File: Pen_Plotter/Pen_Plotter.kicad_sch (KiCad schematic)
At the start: 37 parts, among them J1 USB_Type-C_Breakout, J2 PinHeader_01x05_P2.54mm_Verti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, J3 PinHeader_01x05_P2.54mm_Verti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, J4 Screw_Terminal_01x02_P3.5mm, J5 PinHeader_01x02_P2.54mm_Verti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, J6 PinHeader_01x02_P2.54mm_Verti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, J7 PinHeader_01x03_P2.54mm_Verti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, Q1 Transistor_MOSFET_NCh_SOT23, Q2 Transistor_MOSFET_NCh_SOT23, SW1 Switch_Tactile_Omron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

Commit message: Added some text
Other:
- note added: "ESP32 Wroom Module"
- note added: "Minimum Circuit"
- note added: "Motor 1"
- note added: "Motor 2"
- note added: "Voltage Regulator Circuit"
- moved on the sheet: C1, C2, C3, D1, R1, SW1, U1

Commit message: 6 January
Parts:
- J1: footprint ProshPlay:ProshPlay-Type-C-breakout-board -> Proshplay Type C:ProshPlay-Type-C-breakout-board
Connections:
- no-connect marks 7 -> 17
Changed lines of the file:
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@@
 	)
 	(junction
+		(at 328.93 125.73)
+		(diameter 0)
+		(color 0 0 0 0)
+	)
+	(junction
 		(at 256.54 111.76)
 		(diameter 0)
@@
 		(color 0 0 0 0)
 	)
+	(junction
+		(at 340.7823 109.855)
+		(diameter 0)
+		(color 0 0 0 0)
+	)
 	(no_connect
 		(at 341.63 45.72)
 	)
 	(no_connect
+		(at 195.58 90.17)
+	)
+	(no_connect
+		(at 165.1 82.55)
+	)
+	(no_connect
 		(at 372.11 43.18)
 	)
 	(no_connect
+		(at 195.58 92.71)
+	)
+	(no_connect
 		(at 341.63 66.04)
 	)
 	(no_connect
+		(at 195.58 95.25)
+	)
+	(no_connect
 		(at 341.63 58.42)
 	)
 	(no_connect
+		(at 195.58 97.79)
+	)
+	(no_connect
 		(at 341.63 63.5)
 	)
 	(no_connect
+		(at 195.58 125.73)
+	)
+	(no_connect
+		(at 195.58 130.81)
+	)
+	(no_connect
 		(at 372.11 63.5)
 	)
@@
 		(at 341.63 60.96)
 	)
+	(no_connect
+		(at 165.1 85.09)
+	)
+	(no_connect
+		(at 195.58 87.63)
+	)
+	(no_connect
+		(at 195.58 123.19)
+	)
 	(wire
 		(pts
@@
 	(wire
 		(pts
+			(xy 328.93 125.73) (xy 328.93 126.365)
+		)
+		(stroke
+			(width 0)
+			(type default)
+		)
+	)
+	(wire
+		(pts
 			(xy 260.35 153.67) (xy 264.16 153.67)
 		)
@@
 	(wire
 		(pts
+			(xy 332.74 125.73) (xy 328.93 125.73)
+		)
+		(stroke
+			(width 0)
+			(type default)
+		)
+	)
+	(wire
+		(pts
+			(xy 332.74 129.54) (xy 332.74 125.73)
+		)
+		(stroke
+			(width 0)
+			(type default)
+		)
+	)
+	(wire
+		(pts
 			(xy 337.82 50.8) (xy 341.63 50.8)
 		)
@@
 	(wire
 		(pts
-			(xy 328.93 125.095) (xy 328.93 126.365)
+			(xy 328.93 125.095) (xy 328.93 125.73)
 		)
 		(stroke
@@
 	(wire
 		(pts
+			(xy 340.7823 109.855) (xy 336.55 109.855)
+		)
+		(stroke
+			(width 0)
+			(type default)
+		)
+	)
+	(wire
+		(pts
 			(xy 326.39 125.095) (xy 328.93 125.095)
 		)
@@
 	(wire
 		(pts
-			(xy 344.17 109.855) (xy 336.55 109.855)
+			(xy 344.17 109.855) (xy 340.7823 109.855)
 		)
 		(stroke
@@
 		)
 	)
+	(wire
+		(pts
+			(xy 339.09 129.54) (xy 332.74 129.54)
+		)
+		(stroke
+			(width 0)
+			(type default)
+		)
+	)
 	(global_label "EN"
 		(shape input)
@@
 	(global_label "VDD"
 		(shape input)
-		(at 284.48 30.48 90)
+		(at 284.48 30.48 0)
 		(fields_autoplaced yes)
 		(effects
@@
 		)
 		(property "Intersheetrefs" "${INTERSHEET_REFS}"
-			(at 284.48 23.8662 90)
+			(at 291.0938 30.48 0)
 			(effects
 				(font
@@
 			)
 		)
-		(property "Footprint" "ProshPlay:ProshPlay-Type-C-breakout-board"
+		(property "Footprint" "Proshplay Type C:ProshPlay-Type-C-breakout-board"
 			(at 329.565 120.015 0)
 			(effects
@@
 	)
 	(symbol
+		(lib_id "fab:PWR_FLAG")
+		(at 340.7823 109.855 0)
+		(unit 1)
+		(exclude_from_sim no)
+		(in_bom yes)
+		(on_board yes)
+		(dnp no)
+		(fields_autoplaced yes)
+		(property "Reference" "#FLG01"
+			(at 340.7823 109.855 0)
+			(effects
+				(font
+					(size 1.27 1.27)
+				)
+				(hide yes)
+			)
+		)
+		(property "Value" "PWR_FLAG"
+			(at 340.7823 104.775 0)
+			(effects
+				(font
+					(size 1.27 1.27)
+				)
+			)
+		)
+		(property "Footprint" ""
+			(at 340.7823 109.855 0)
+			(effects
+				(font
+					(size 1.27 1.27)
+				)
+				(hide yes)
+			)
+		)
+		(property "Datasheet" "~"
+			(at 340.7823 109.855 0)
+			(effects
+				(font
+					(size 1.27 1.27)
+				)
+				(hide yes)
+			)
+		)
+		(property "Description" "Special symbol for telling ERC where power comes from"
+			(at 340.7823 109.855 0)
+			(effects
+				(font
+					(size 1.27 1.27)
+				)
+				(hide yes)
+			)
+		)
+		(pin "1"
+		)
+		(instances
+			(project ""
+				(path "/4e9b223a-cbc5-44ea-8094-5eb0dbc835d2"
+					(reference "#FLG01")
+					(unit 1)
+				)
+			)
+		)
+	)
+	(symbol
 		(lib_id "fab:Transistor_MOSFET_NCh_SOT23")
 		(at 378.46 101.6 0)
@@
 					(unit 1)
 				)
+			)
+		)
+	)
+	(symbol
+		(lib_id "fab:PWR_FLAG")
+		(at 339.09 129.54 0)
+		(unit 1)
+		(exclude_from_sim no)
+		(in_bom yes)
+		(on_board yes)
+		(dnp no)
+		(fields_autoplaced yes)
+		(property "Reference" "#FLG02"
+			(at 339.09 129.54 0)
+			(effects
+				(font
+					(size 1.27 1.27)
+				)
+				(hide yes)
+			)
+		)
+		(property "Value" "PWR_FLAG"
+			(at 339.09 124.46 0)
+			(effects
+				(font
+					(size 1.27 1.27)
+				)
+			)
+		)
+		(property "Footprint" ""
+			(at 339.09 129.54 0)
+			(effects
+				(font
+					(size 1.27 1.27)
+				)
+				(hide yes)
+			)
+		)
+		(property "Datasheet" "~"
+			(at 339.09 129.54 0)
+			(effects
+				(font
+					(size 1.27 1.27)
+				)
+				(hide yes)
+			)
+		)
+		(property "Description" "Special symbol for telling ERC where power comes from"
+			(at 339.09 129.54 0)
+			(effects
+				(font
+					(size 1.27 1.27)
+				)
+				(hide yes)
+			)
+		)
+		(pin "1"
+		)
+		(instances
+			(project "Pen_Plotter"
+				(path "/4e9b223a-cbc5-44ea-8094-5eb0dbc835d2"
+					(reference "#FLG02")
+					(unit 1)
+				)

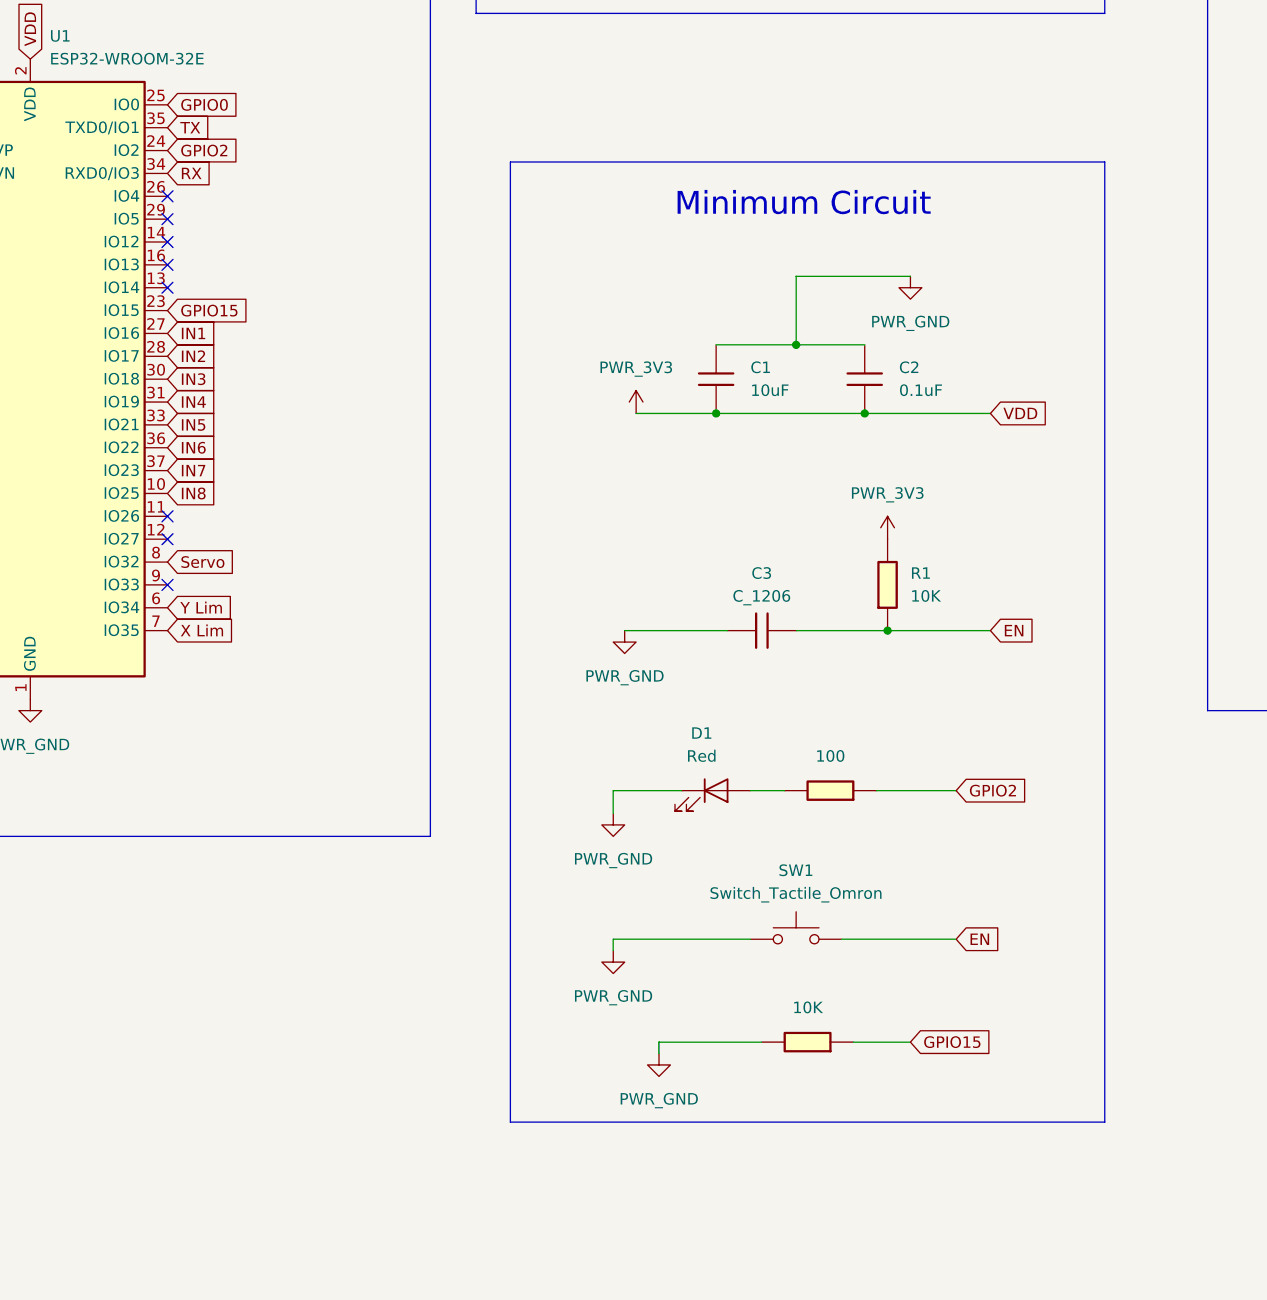
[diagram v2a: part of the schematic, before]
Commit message: Wired THT Components
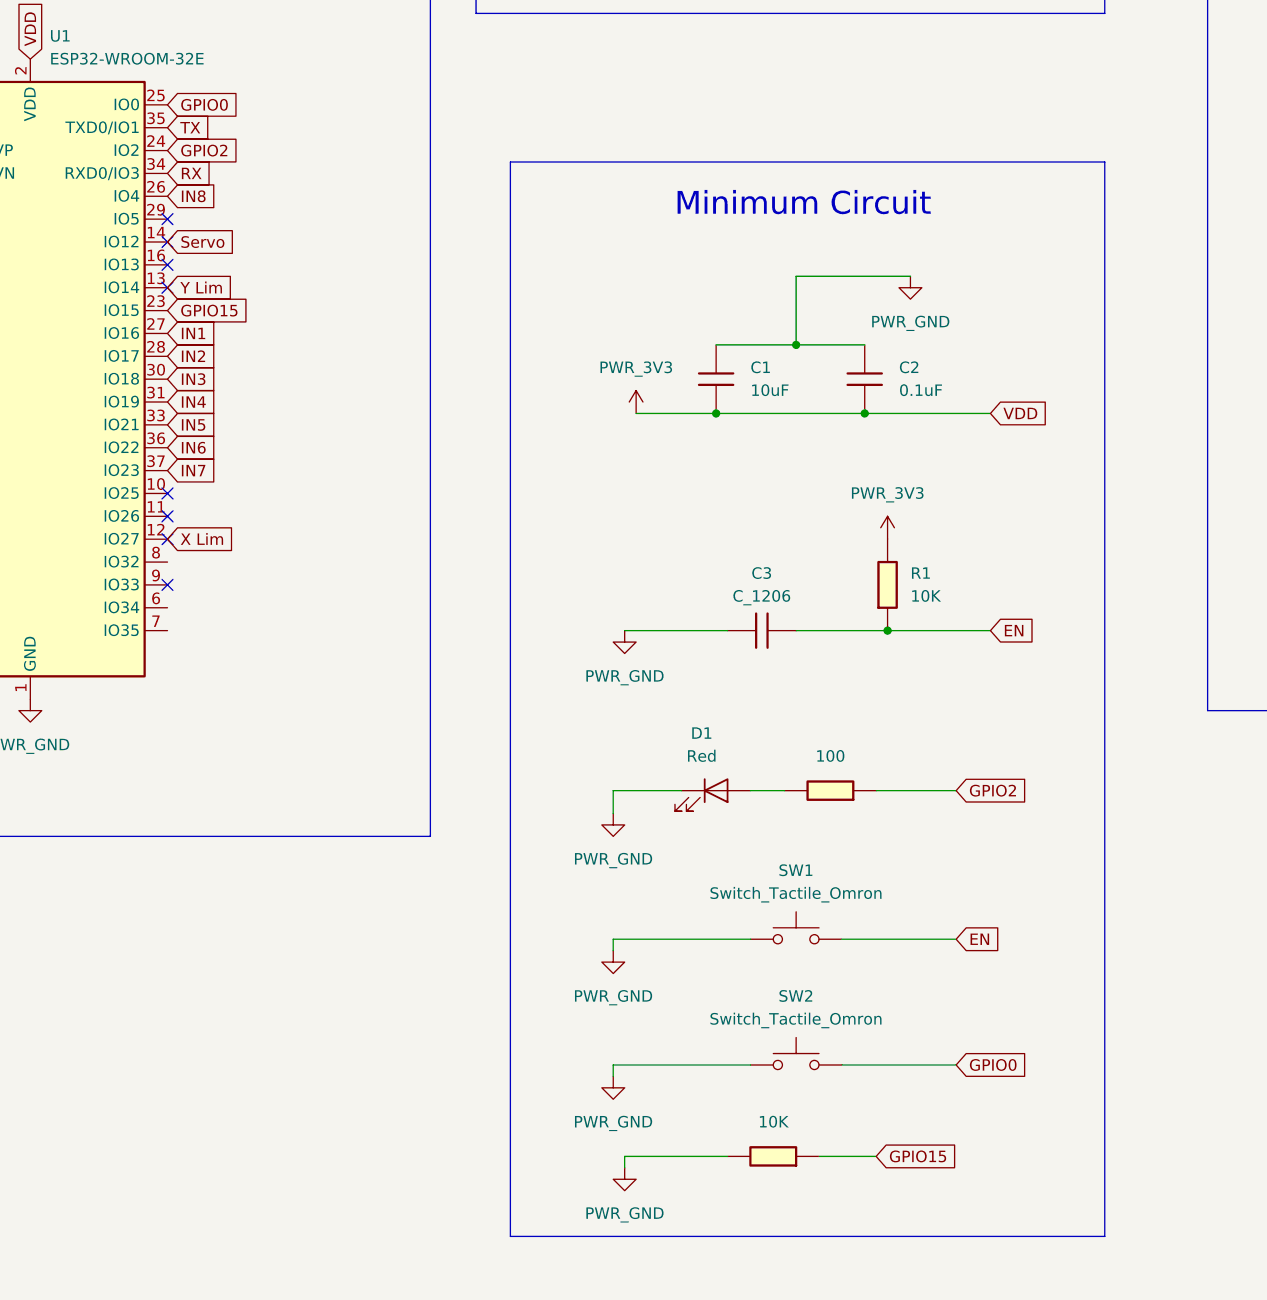
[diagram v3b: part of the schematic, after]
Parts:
- added SW2: Switch_Tactile_Omron, fab:Button_Omron_B3SN_6.0x6.0mm, symbol fab:Switch_Tactile_Omron
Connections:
- net GPIO0: now also SW2.2
- net IN8: now also U1.26 (IO4); no longer U1.10 (IO25)
- net PWR_GND: now also SW2.1
- net Servo: now also U1.14 (IO12); no longer U1.8 (IO32)
- net X Lim: now also U1.12 (IO27); no longer U1.7 (IO35)
- net Y Lim: now also U1.13 (IO14); no longer U1.6 (IO34)
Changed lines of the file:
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@@
 	(rectangle
 		(start 233.68 83.82)
-		(end 299.72 190.5)
+		(end 299.72 203.2)
 		(stroke
 			(width 0)
@@
 	)
 	(no_connect
+		(at 195.58 120.65)
+	)
+	(no_connect
 		(at 341.63 58.42)
 	)
 	(no_connect
+		(at 195.58 123.19)
+	)
+	(no_connect
 		(at 195.58 97.79)
 	)
@@
 		(at 165.1 85.09)
 	)
-	(no_connect
-		(at 195.58 87.63)
-	)
-	(no_connect
-		(at 195.58 123.19)
+	(wire
+		(pts
+			(xy 245.11 184.15) (xy 245.11 185.42)
+		)
+		(stroke
+			(width 0)
+			(type default)
+		)
 	)
 	(wire
@@
 	(wire
 		(pts
+			(xy 270.51 184.15) (xy 283.21 184.15)
+		)
+		(stroke
+			(width 0)
+			(type default)
+		)
+	)
+	(wire
+		(pts
 			(xy 254 35.56) (xy 254 41.91)
 		)
@@
 	(wire
 		(pts
-			(xy 250.19 181.61) (xy 261.62 181.61)
+			(xy 246.38 194.31) (xy 257.81 194.31)
 		)
 		(stroke
@@
 	(wire
 		(pts
-			(xy 250.19 182.88) (xy 250.19 181.61)
+			(xy 246.38 195.58) (xy 246.38 194.31)
 		)
 		(stroke
@@
 	(wire
 		(pts
+			(xy 260.35 184.15) (xy 245.11 184.15)
+		)
+		(stroke
+			(width 0)
+			(type default)
+		)
+	)
+	(wire
+		(pts
 			(xy 49.53 143.51) (xy 49.53 146.05)
 		)
@@
 	(wire
 		(pts
-			(xy 271.78 181.61) (xy 278.13 181.61)
+			(xy 267.97 194.31) (xy 274.32 194.31)
 		)
 		(stroke
@@
 	(global_label "Servo"
 		(shape input)
-		(at 195.58 128.27 0)
+		(at 195.58 92.71 0)
 		(fields_autoplaced yes)
 		(effects
@@
 		)
 		(property "Intersheetrefs" "${INTERSHEET_REFS}"
-			(at 203.7661 128.27 0)
+			(at 203.7661 92.71 0)
 			(effects
 				(font
@@
 		)
 	)
-	(global_label "IN8"
-		(shape input)
-		(at 195.58 120.65 0)
-		(fields_autoplaced yes)
-		(effects
-			(font
-				(size 1.27 1.27)
-			)
-			(justify left)
-		)
-		(property "Intersheetrefs" "${INTERSHEET_REFS}"
-			(at 201.71 120.65 0)
-			(effects
-				(font
-					(size 1.27 1.27)
-				)
-				(justify left)
-				(hide yes)
-			)
-		)
-	)
 	(global_label "OUT4"
 		(shape input)
@@
 		)
 	)
+	(global_label "IN8"
+		(shape input)
+		(at 195.58 87.63 0)
+		(fields_autoplaced yes)
+		(effects
+			(font
+				(size 1.27 1.27)
+			)
+			(justify left)
+		)
+		(property "Intersheetrefs" "${INTERSHEET_REFS}"
+			(at 201.71 87.63 0)
+			(effects
+				(font
+					(size 1.27 1.27)
+				)
+				(justify left)
+				(hide yes)
+			)
+		)
+	)
 	(global_label "IN4"
 		(shape input)
@@
 		)
 	)
+	(global_label "GPIO0"
+		(shape input)
+		(at 283.21 184.15 0)
+		(fields_autoplaced yes)
+		(effects
+			(font
+				(size 1.27 1.27)
+			)
+			(justify left)
+		)
+		(property "Intersheetrefs" "${INTERSHEET_REFS}"
+			(at 291.88 184.15 0)
+			(effects
+				(font
+					(size 1.27 1.27)
+				)
+				(justify left)
+				(hide yes)
+			)
+		)
+	)
 	(global_label "Y Lim"
 		(shape input)
-		(at 195.58 133.35 0)
+		(at 195.58 97.79 0)
 		(fields_autoplaced yes)
 		(effects
@@
 		)
 		(property "Intersheetrefs" "${INTERSHEET_REFS}"
-			(at 203.9476 133.35 0)
+			(at 203.9476 97.79 0)
 			(effects
 				(font
@@
 	(global_label "GPIO15"
 		(shape input)
-		(at 278.13 181.61 0)
+		(at 274.32 194.31 0)
 		(fields_autoplaced yes)
 		(effects
@@
 		)
 		(property "Intersheetrefs" "${INTERSHEET_REFS}"
-			(at 288.0095 181.61 0)
+			(at 284.1995 194.31 0)
 			(effects
 				(font
@@
 	(global_label "X Lim"
 		(shape input)
-		(at 195.58 135.89 0)
+		(at 195.58 125.73 0)
 		(fields_autoplaced yes)
 		(effects
@@
 		)
 		(property "Intersheetrefs" "${INTERSHEET_REFS}"
-			(at 204.0685 135.89 0)
+			(at 204.0685 125.73 0)
 			(effects
 				(font
@@
 	(symbol
 		(lib_id "fab:PWR_GND")
-		(at 250.19 182.88 0)
+		(at 246.38 195.58 0)
 		(unit 1)
 		(exclude_from_sim no)
@@
 		(fields_autoplaced yes)
 		(property "Reference" "#PWR017"
-			(at 250.19 189.23 0)
+			(at 246.38 201.93 0)
 			(effects
 				(font
@@
 		)
 		(property "Value" "PWR_GND"
-			(at 250.19 187.96 0)
+			(at 246.38 200.66 0)
 			(effects
 				(font
@@
 		)
 		(property "Footprint" ""
-			(at 250.19 182.88 0)
+			(at 246.38 195.58 0)
 			(effects
 				(font
@@
 		)
 		(property "Datasheet" ""
-			(at 250.19 182.88 0)
+			(at 246.38 195.58 0)
 			(effects
 				(font
@@
 		)
 		(property "Description" "Power symbol creates a global label with name \"GND\" , ground"
-			(at 250.19 182.88 0)
+			(at 246.38 195.58 0)
 			(effects
 				(font
@@
 	)
 	(symbol
+		(lib_id "fab:Switch_Tactile_Omron")
+		(at 265.43 184.15 0)
+		(unit 1)
+		(exclude_from_sim no)
+		(in_bom yes)
+		(on_board yes)
+		(dnp no)
+		(fields_autoplaced yes)
+		(property "Reference" "SW2"
+			(at 265.43 176.53 0)
+			(effects
+				(font
+					(size 1.27 1.27)
+				)
+			)
+		)
+		(property "Value" "Switch_Tactile_Omron"
+			(at 265.43 179.07 0)
+			(effects
+				(font
+					(size 1.27 1.27)
+				)
+			)
+		)
+		(property "Footprint" "fab:Button_Omron_B3SN_6.0x6.0mm"
+			(at 265.43 184.15 0)
+			(effects
+				(font
+					(size 1.27 1.27)
+				)
+				(hide yes)
+			)
+		)
+		(property "Datasheet" "https://omronfs.omron.com/en_US/ecb/products/pdf/en-b3sn.pdf"
+			(at 265.43 184.15 0)
+			(effects
+				(font
+					(size 1.27 1.27)
+				)
+				(hide yes)
+			)
+		)
+		(property "Description" "Push button switch, Omron, B3SN, Sealed Tactile Switch (SMT), SPST-NO Top Actuated Surface Mount"
+			(at 265.43 184.15 0)
+			(effects
+				(font
+					(size 1.27 1.27)
+				)
+				(hide yes)
+			)
+		)
+		(pin "1"
+		)
+		(pin "2"
+		)
+		(instances
+			(project "Pen_Plotter"
+				(path "/4e9b223a-cbc5-44ea-8094-5eb0dbc835d2"
+					(reference "SW2")
+					(unit 1)
+				)
+			)
+		)
+	)
+	(symbol
 		(lib_id "fab:LED_1206")
 		(at 337.82 67.31 90)
@@
 	(symbol
 		(lib_id "fab:R_1206")
-		(at 266.7 181.61 90)
+		(at 262.89 194.31 90)
 		(unit 1)
 		(exclude_from_sim no)
@@
 		(fields_autoplaced yes)
 		(property "Reference" "R8"
-			(at 266.7 175.26 90)
+			(at 262.89 187.96 90)
 			(effects
 				(font
@@
 		)
 		(property "Value" "10K"
-			(at 266.7 177.8 90)
+			(at 262.89 190.5 90)
 			(effects
 				(font
@@
 		)
 		(property "Footprint" "fab:R_1206"
-			(at 266.7 181.61 90)
+			(at 262.89 194.31 90)
 			(effects
 				(font
@@
 		)
 		(property "Datasheet" "~"
-			(at 266.7 181.61 0)
+			(at 262.89 194.31 0)
 			(effects
 				(font
@@
 		)
 		(property "Description" "Resistor"
-			(at 266.7 181.61 0)
+			(at 262.89 194.31 0)
 			(effects
 				(font
@@
 					(unit 1)
 				)
+			)
+		)
+	)
+	(symbol
+		(lib_id "fab:PWR_GND")
+		(at 245.11 185.42 0)
+		(unit 1)
+		(exclude_from_sim no)
+		(in_bom yes)
+		(on_board yes)
+		(dnp no)
+		(fields_autoplaced yes)
+		(property "Reference" "#PWR033"
+			(at 245.11 191.77 0)
+			(effects
+				(font
+					(size 1.27 1.27)
+				)
+				(hide yes)
+			)
+		)
+		(property "Value" "PWR_GND"
+			(at 245.11 190.5 0)
+			(effects
+				(font
+					(size 1.27 1.27)
+				)
+			)
+		)
+		(property "Footprint" ""
+			(at 245.11 185.42 0)
+			(effects
+				(font
+					(size 1.27 1.27)
+				)
+				(hide yes)
+			)
+		)
+		(property "Datasheet" ""
+			(at 245.11 185.42 0)
+			(effects
+				(font
+					(size 1.27 1.27)
+				)
+				(hide yes)
+			)
+		)
+		(property "Description" "Power symbol creates a global label with name \"GND\" , ground"
+			(at 245.11 185.42 0)
+			(effects
+				(font
+					(size 1.27 1.27)
+				)
+				(hide yes)
+			)
+		)
+		(pin "1"
+		)
+		(instances
+			(project "Pen_Plotter"
+				(path "/4e9b223a-cbc5-44ea-8094-5eb0dbc835d2"
+					(reference "#PWR033")
+					(unit 1)
+				)
